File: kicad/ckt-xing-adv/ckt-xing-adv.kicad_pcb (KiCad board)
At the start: 2 copper layers, 127 x 76.2 mm, 135 parts, among them J1 Screw_Terminal_01x02, J10 SM04B-SRSS, J11 SM04B-SRSS, J12 SM04B-SRSS, J13 Conn_02x03_Row_Letter_First, J14 Conn_02x03_Row_Letter_First, J15 Conn_02x05_Counter_Clockwise, J16 SM04B-SRSS, J17 Screw_Terminal_01x02, J18 Screw_Terminal_01x02, J2 Screw_Terminal_01x02, J3 Screw_Terminal_01x02, J4 SM04B-SRSS, J5 SM04B-SRSS, J6 SM04B-SRSS, J7 SM04B-SRSS, J8 SM04B-SRSS, J9 SM04B-SRSS, Q1 ZXMS6004FF, Q2 ZXMS6004FF, Q3 ZXMS6004FF, SW1 FSM4JSMATR, SW2 FSM4JSMATR, SW3 FSM4JSMATR, U1 AP7381-33Y, U2 AP63205WU, U3 W25Q128JVS, U4 ATtiny861A-S, U5 PCA9685PW, U6 PCA9555D, U7 PAM8301, U8 DRV8231A, U9 DRV8231A

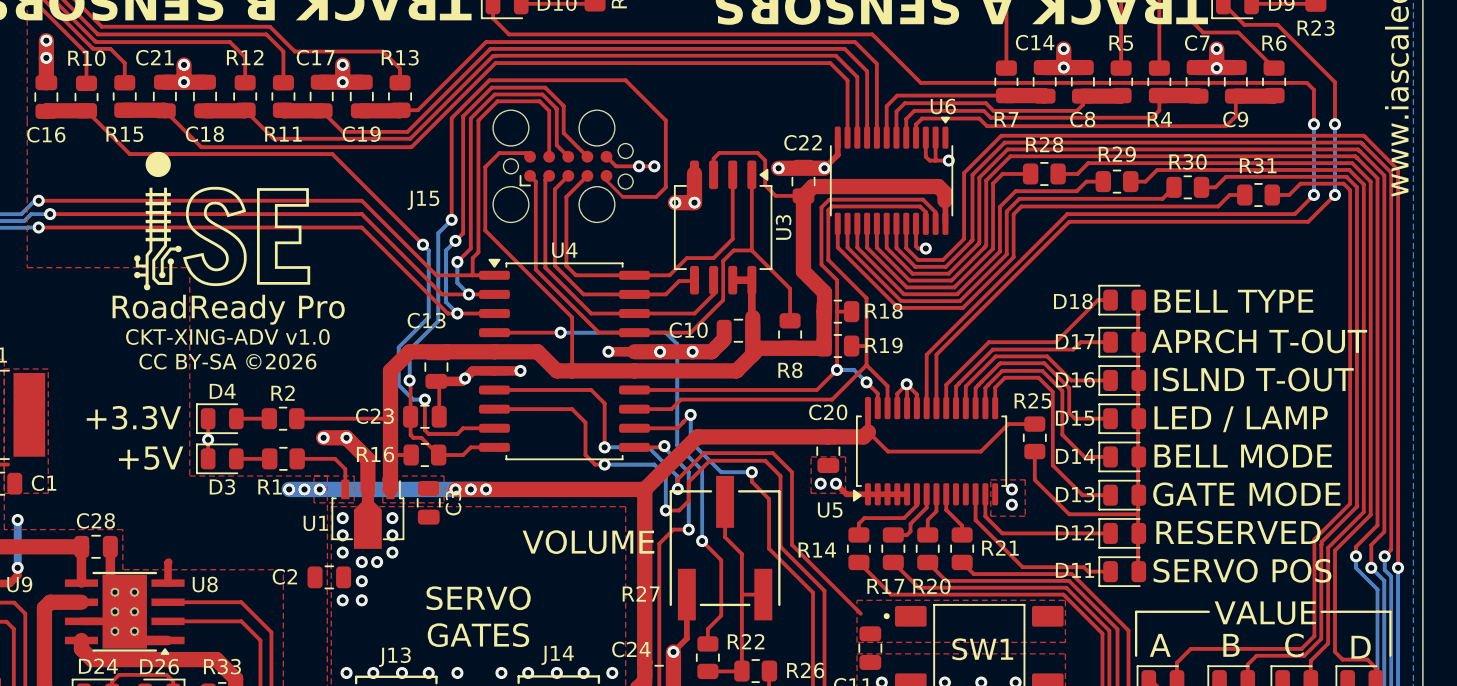
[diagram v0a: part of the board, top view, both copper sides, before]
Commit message: Update to v1.1, adding level shifters between the CPU and the 9685, since it's in the 5V domain
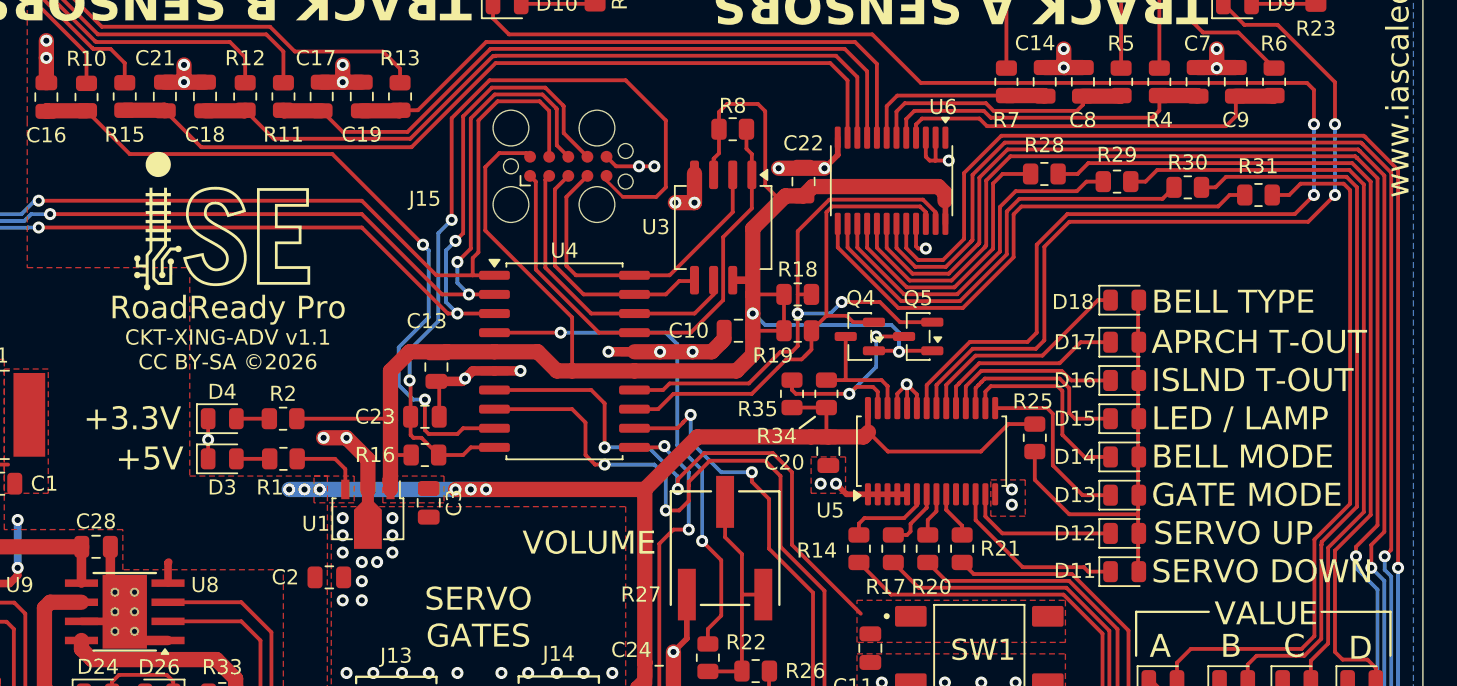
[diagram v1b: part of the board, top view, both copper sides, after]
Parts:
- added Q4: BSS138, Package_TO_SOT_SMD:SOT-23, F.Cu at (115.0, 57.1)
- added Q5: BSS138, Package_TO_SOT_SMD:SOT-23, F.Cu at (118.9, 57.1)
- added R34: 10k, Resistor_SMD:R_0805_2012Metric, F.Cu at (112.8, 61.0)
- added R35: 10k, Resistor_SMD:R_0805_2012Metric, F.Cu at (110.5, 61.0)
- moved R8 14.2 mm to (106.6, 43.4), turned to 0 degrees
- moved R18 2.90 mm to (110.9, 54.4)
- moved R19 2.85 mm to (110.9, 56.8)
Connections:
- U5 pad 26: /SCL -> Net-(Q4-D)
- U5 pad 27: /SDA -> Net-(Q5-D)
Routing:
- net +3.3V: track 104.5 -> 123.0 mm, vias 0 -> 2
- net Net-(Q5-D): track 0.00 -> 14.3 mm, vias 0 -> 2
- net Net-(Q4-D): track 0.00 -> 8.34 mm
- net /SCL: track 39.9 -> 34.5 mm
- net +5V: track 154.7 -> 159.2 mm
- net Net-(D13-K): track 15.4 -> 12.1 mm
- net /~{FLASH_CS}: track 37.0 -> 33.7 mm
- net Net-(D9-K): track 51.5 -> 53.9 mm
- net Net-(D10-K): track 98.1 -> 100.4 mm
- net /SDA: track 39.4 -> 41.6 mm
- net /FLASH_MISO: track 23.1 -> 22.1 mm
- net Net-(D14-K): track 14.2 -> 13.2 mm
- net Net-(D15-K): track 13.5 -> 12.6 mm
- net Net-(D16-K): track 12.5 -> 11.7 mm
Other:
- board text added: "CKT-XING-ADV v1.1 CC BY-SA ©2026"
- board text added: "SERVO DOWN"
- board text added: "SERVO UP"
- board text removed: "CKT-XING-ADV v1.0 CC BY-SA ©2026"
- board text removed: "RESERVED"
- board text removed: "SERVO POS"

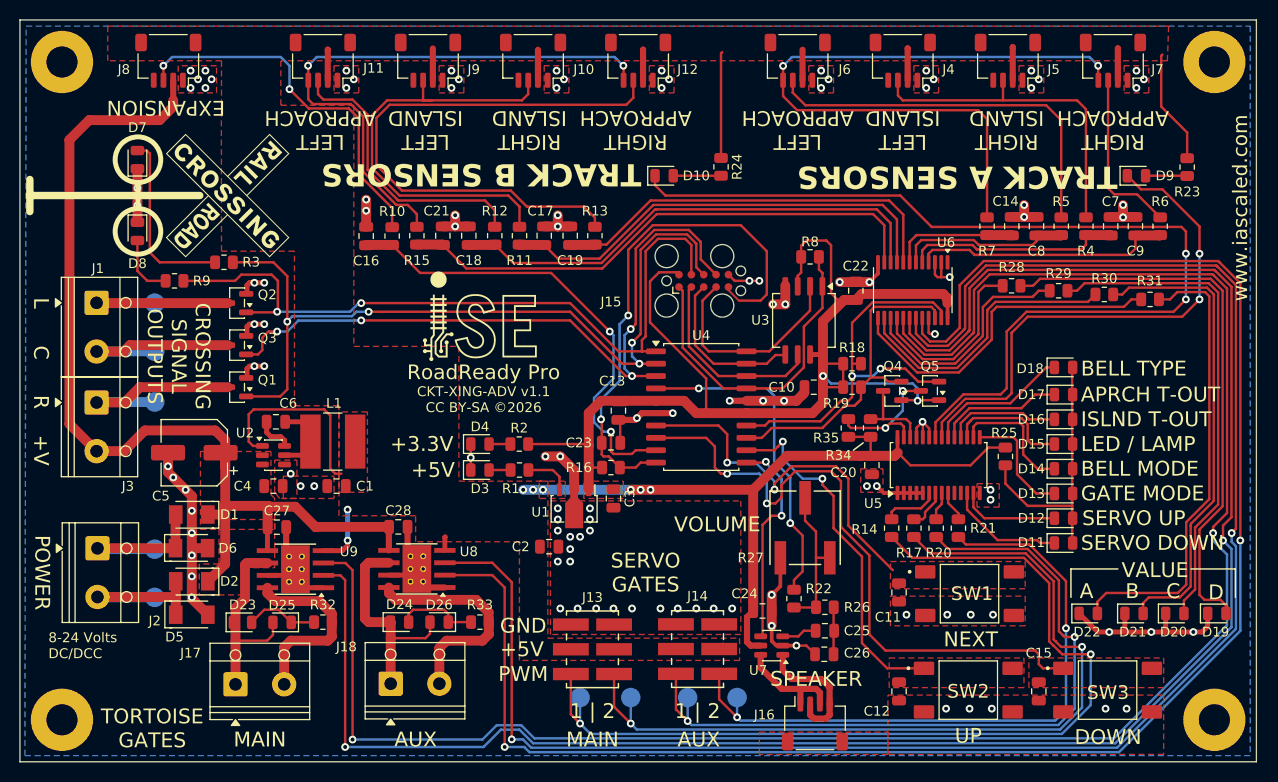
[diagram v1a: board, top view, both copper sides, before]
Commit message: Add electrolytic to servo drivers
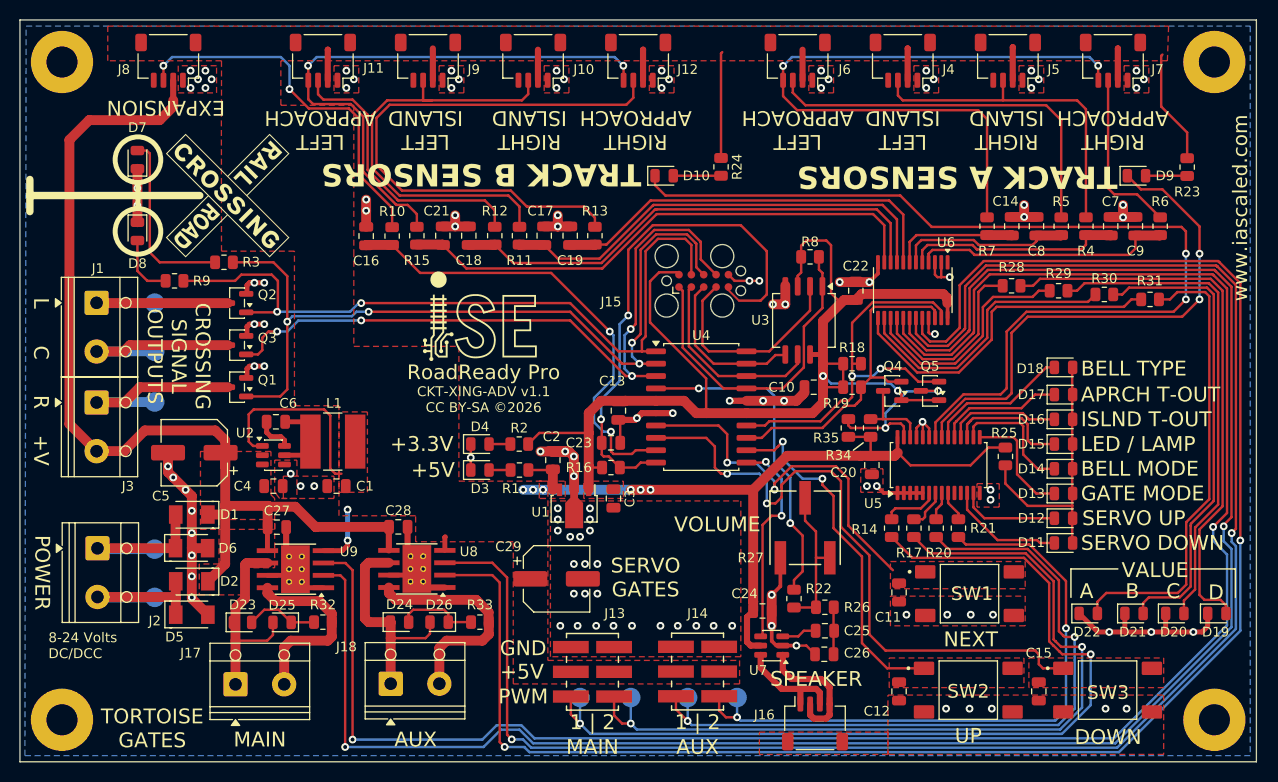
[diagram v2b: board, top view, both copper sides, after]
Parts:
- added C29: 220uF 6.3V, Capacitor_SMD:CP_Elec_6.3x5.8, F.Cu at (80.5, 76.5)
- moved C2 8.90 mm to (80.1, 64.3), turned to 90 degrees
- moved J13 2.31 mm to (84.2, 86.0)
- moved J14 2.31 mm to (95.0, 86.0)
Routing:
- net GND: track 163.6 -> 168.2 mm, vias 116 -> 121
- net Net-(Q5-D): track 14.3 -> 17.6 mm
- net Net-(J14-Pin_a1): track 77.3 -> 75.0 mm
- net Net-(J13-Pin_a1): track 96.4 -> 94.1 mm
- net Net-(J14-Pin_b1): track 67.8 -> 65.8 mm
- net Net-(J13-Pin_b1): track 87.7 -> 85.9 mm
- net +3.3V: track 123.0 -> 122.3 mm
- net +5V: track 159.2 -> 158.5 mm
